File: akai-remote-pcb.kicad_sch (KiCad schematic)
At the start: 14 parts, among them J1 Conn_01x11, Q1 T2N7002AK, Q2 T2N7002AK, Q3 T2N7002AK, Q4 T2N7002AK, Q5 T2N7002AK, Q6 T2N7002AK, Q7 T2N7002AK, U1 MOUDLE-SEEEDUINO-XIAO-ESP32C3

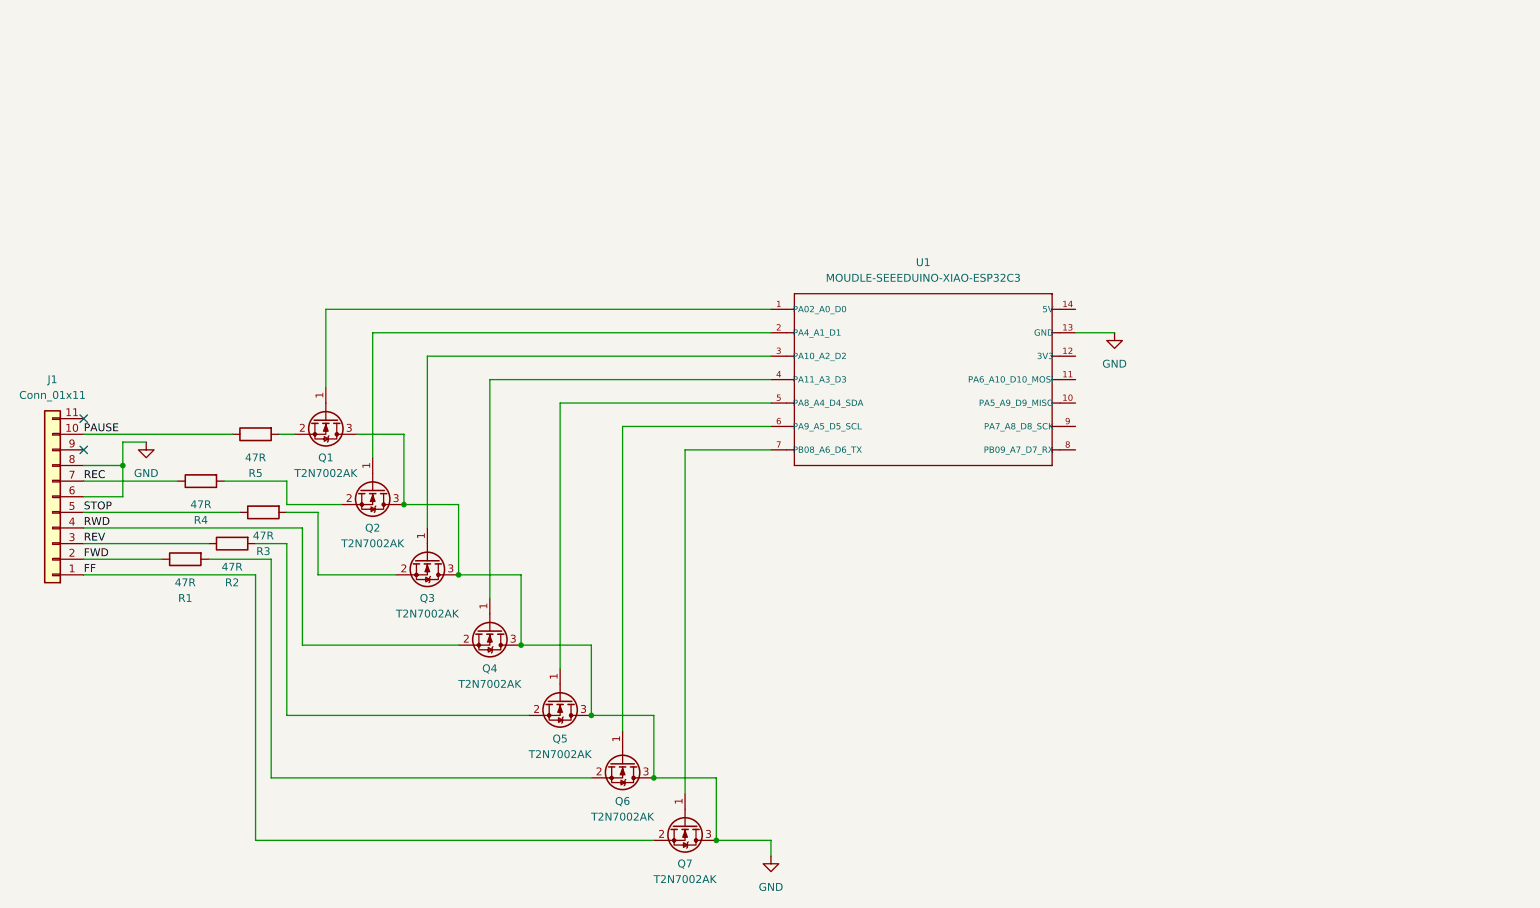
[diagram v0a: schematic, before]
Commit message: Fix MOSFET direction and add external pull-down resistors
This commit fixes the direction of the MOSFETs and adds external
pull-down resistors to their gates to prevent undefined behavior when
the ESP is not powered.
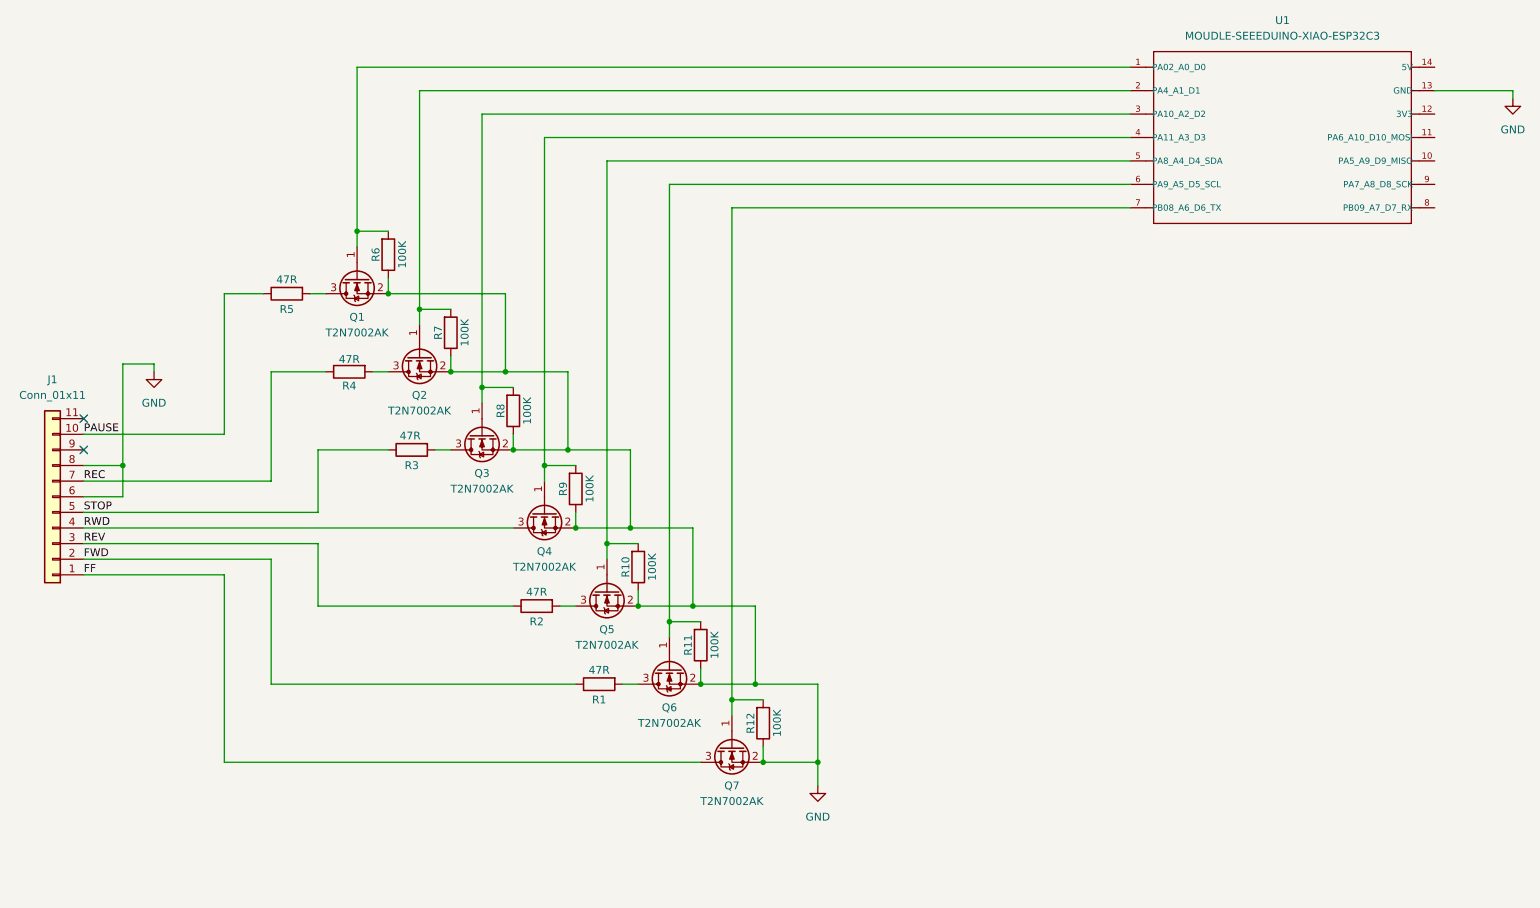
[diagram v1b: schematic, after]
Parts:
- added R10, R11, R12, R6, R7, R8, R9: 100K, Resistor_SMD:R_0603_1608Metric, symbol Device:R
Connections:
- net FF: now also Q7.3 (D); no longer Q7.2 (S)
- net GND: now also Q1.2 (S), Q2.2 (S), Q3.2 (S), Q4.2 (S), Q5.2 (S), Q6.2 (S), Q7.2 (S), R10.1, R11.1, R12.1, R6.1, R7.1, R8.1, R9.1; no longer Q1.3 (D), Q2.3 (D), Q3.3 (D), Q4.3 (D), Q5.3 (D), Q6.3 (D), Q7.3 (D)
- net RWD: now also Q4.3 (D); no longer Q4.2 (S)
- net at R5.2: now also Q1.3 (D); no longer Q1.2 (S)
- net at Q3.1 (G), U1.3 (PA10_A2_D2): now also R8.2
- net at R3.2: now also Q3.3 (D); no longer Q3.2 (S)
- net at Q2.1 (G), U1.2 (PA4_A1_D1): now also R7.2
- net at R4.2: now also Q2.3 (D); no longer Q2.2 (S)
- net at Q6.1 (G), U1.6 (PA9_A5_D5_SCL): now also R11.2
- net at R1.2: now also Q6.3 (D); no longer Q6.2 (S)
- net at Q1.1 (G), U1.1 (PA02_A0_D0): now also R6.2
- net at Q4.1 (G), U1.4 (PA11_A3_D3): now also R9.2
- net at Q5.1 (G), U1.5 (PA8_A4_D4_SDA): now also R10.2
- net at Q7.1 (G), U1.7 (PB08_A6_D6_TX): now also R12.2
- net at R2.2: now also Q5.3 (D); no longer Q5.2 (S)
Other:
- company: (none) -> Funkeleinhorn
- title: (none) -> Akai GX 635 Remote
- moved on the sheet: Q1, Q2, Q3, Q4, Q5, Q6, Q7, R1, R2, R3, R4, R5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

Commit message: Fix remote connector pinout, rework routing for cleaner design
This commit fixes the pinout of the Akai GX 635 remote connector
which was wrong in older revisions. To allow for cleaner routing
the wiring of remote connector pins to the MOSFETs was changed.
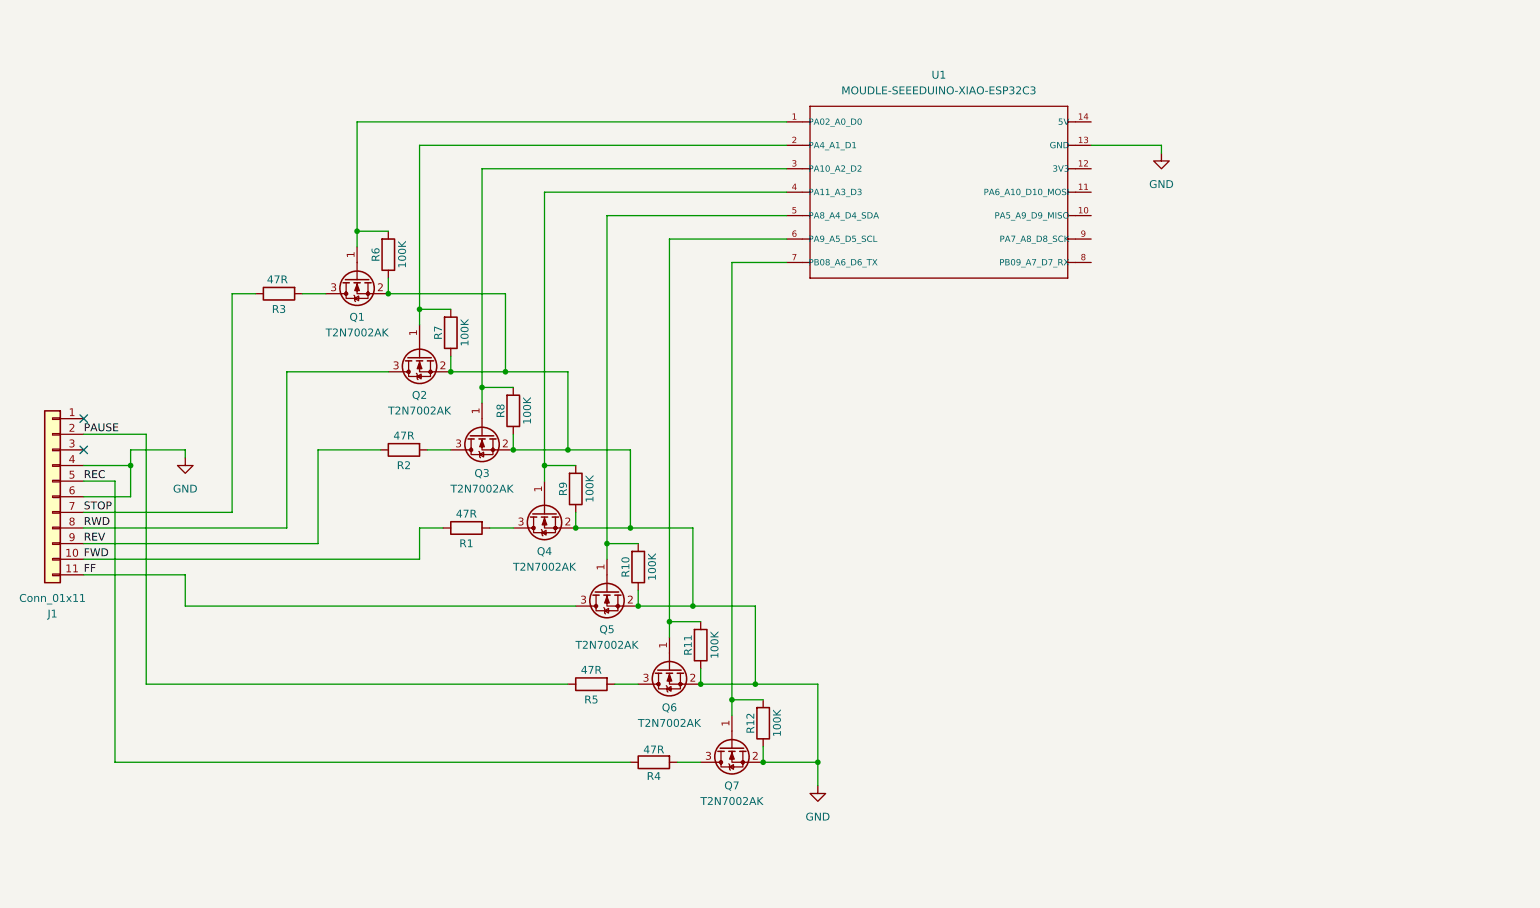
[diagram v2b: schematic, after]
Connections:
- net FF: now also J1.11 (Pin_11), Q5.3 (D); no longer J1.1 (Pin_1), Q7.3 (D)
- net FWD: now also J1.10 (Pin_10); no longer J1.2 (Pin_2)
- net GND: now also J1.4 (Pin_4); no longer J1.8 (Pin_8)
- net PAUSE: now also J1.2 (Pin_2); no longer J1.10 (Pin_10)
- net REC: now also J1.5 (Pin_5); no longer J1.7 (Pin_7)
- net REV: now also J1.9 (Pin_9); no longer J1.3 (Pin_3)
- net RWD: now also J1.8 (Pin_8), Q2.3 (D); no longer J1.4 (Pin_4), Q4.3 (D)
- net STOP: now also J1.7 (Pin_7); no longer J1.5 (Pin_5)
- net at R5.2: now also Q6.3 (D); no longer Q1.3 (D)
- net at Q3.3 (D): now also R2.2; no longer R3.2
- net at R4.2: now also Q7.3 (D); no longer Q2.3 (D)
- net at R1.2: now also Q4.3 (D); no longer Q6.3 (D)
- new net: Q1.3 (D), R3.2
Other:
- moved on the sheet: J1, R1, R2, R3, R4, R5, U1
